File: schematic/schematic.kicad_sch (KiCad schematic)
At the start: 16 parts, among them J1 Conn_01x04, J2 Conn_01x04, J3 Conn_01x04, J4 Conn_01x04, M1 Motor_DC, M2 Motor_DC, M3 Motor_DC, M4 Motor_DC, M5 Motor_Servo, M6 Motor_Servo, U1 BPR-105, U2 BPR-105, U3 BPR-105, U4 BPR-105, U5 LSM9DS1

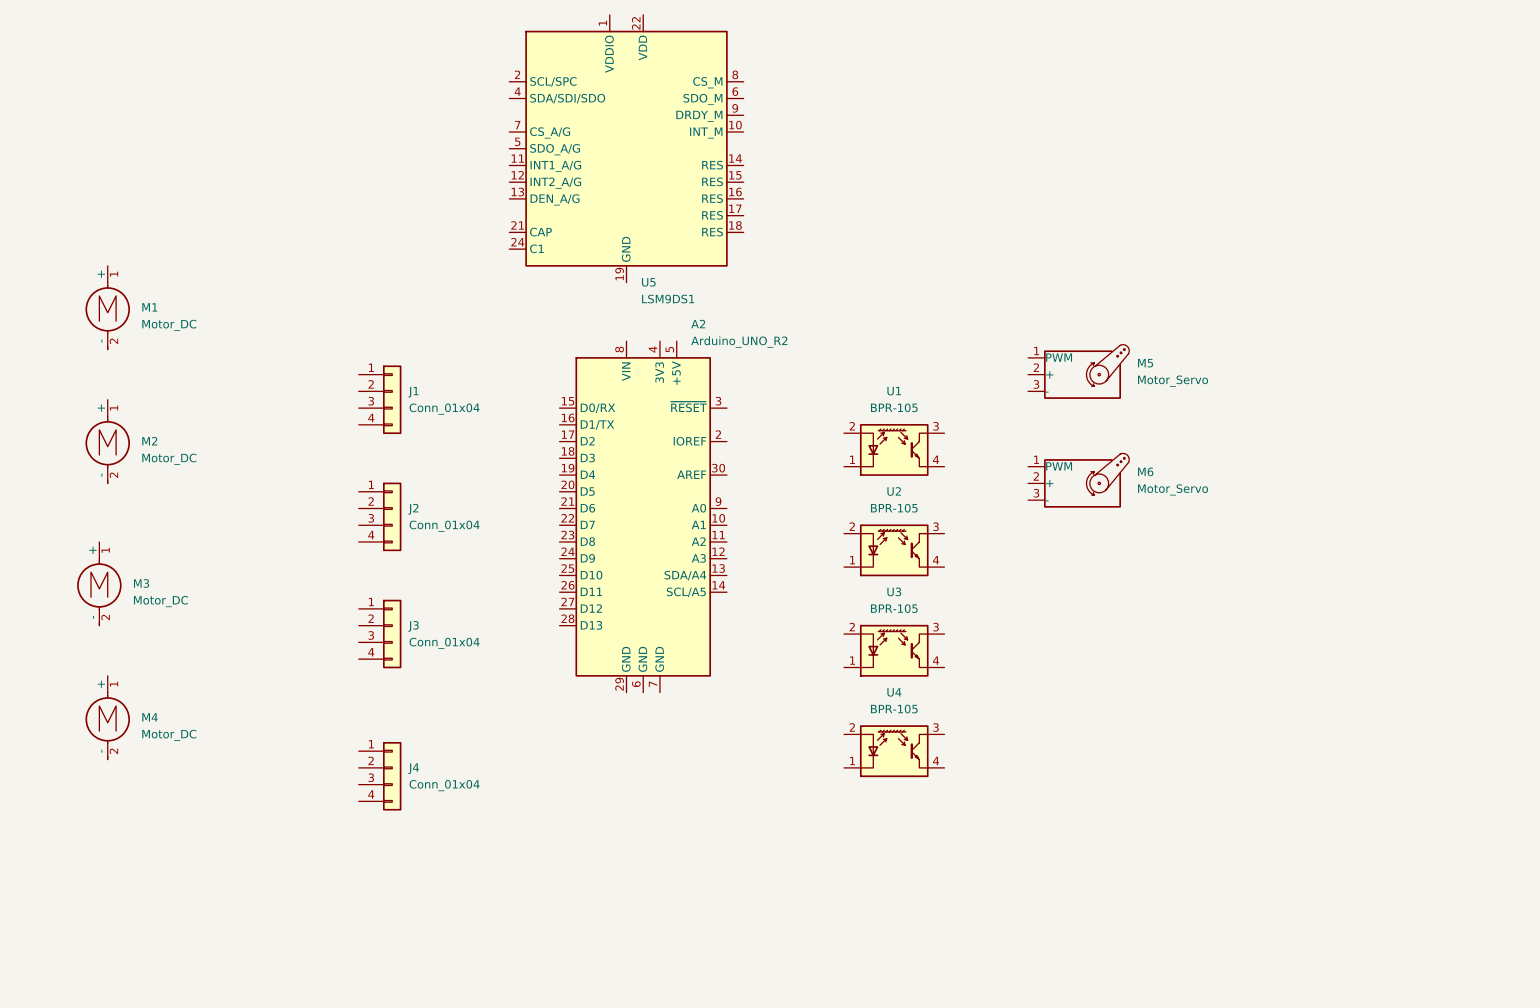
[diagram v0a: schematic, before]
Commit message: added custom symbols for clarity
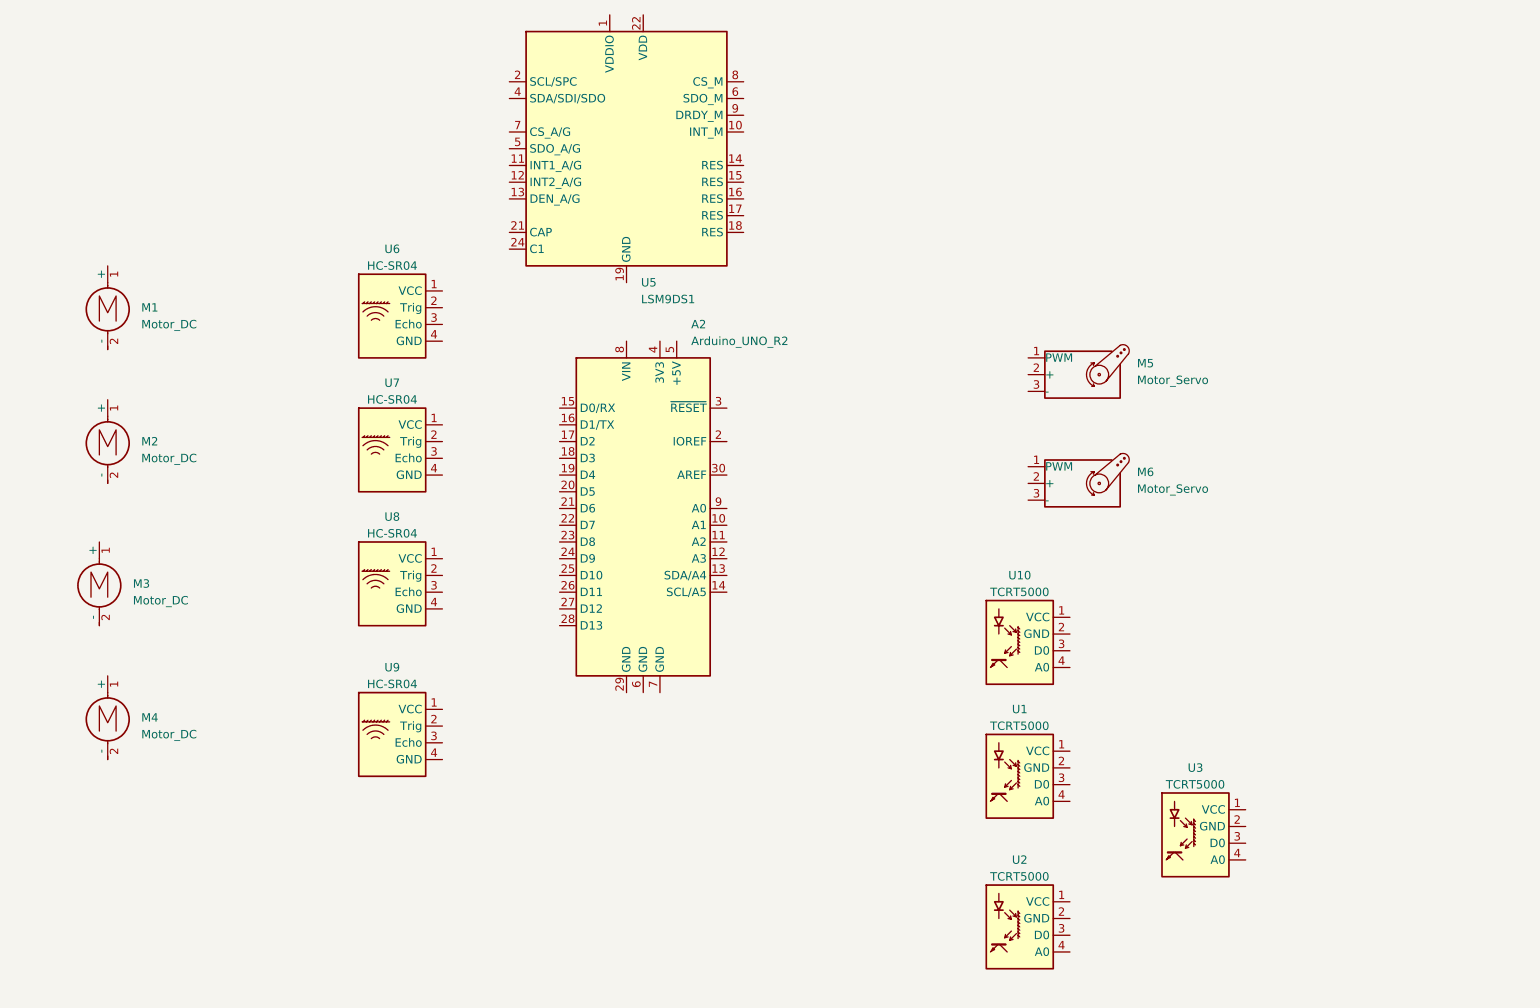
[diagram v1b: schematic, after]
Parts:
- removed J1, J2, J3, J4: Conn_01x04, symbol Connector_Generic:Conn_01x04
- removed U1, U2, U3, U4: BPR-105, OptoDevice:Everlight_ITR8307, symbol Sensor_Proximity:BPR-105
- added U1, U10, U2, U3: TCRT5000, symbol symbol_lib:TCRT5000
- added U6, U7, U8, U9: HC-SR04, symbol symbol_lib:HC-SR04

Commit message: schematic first iter. Running out of pins
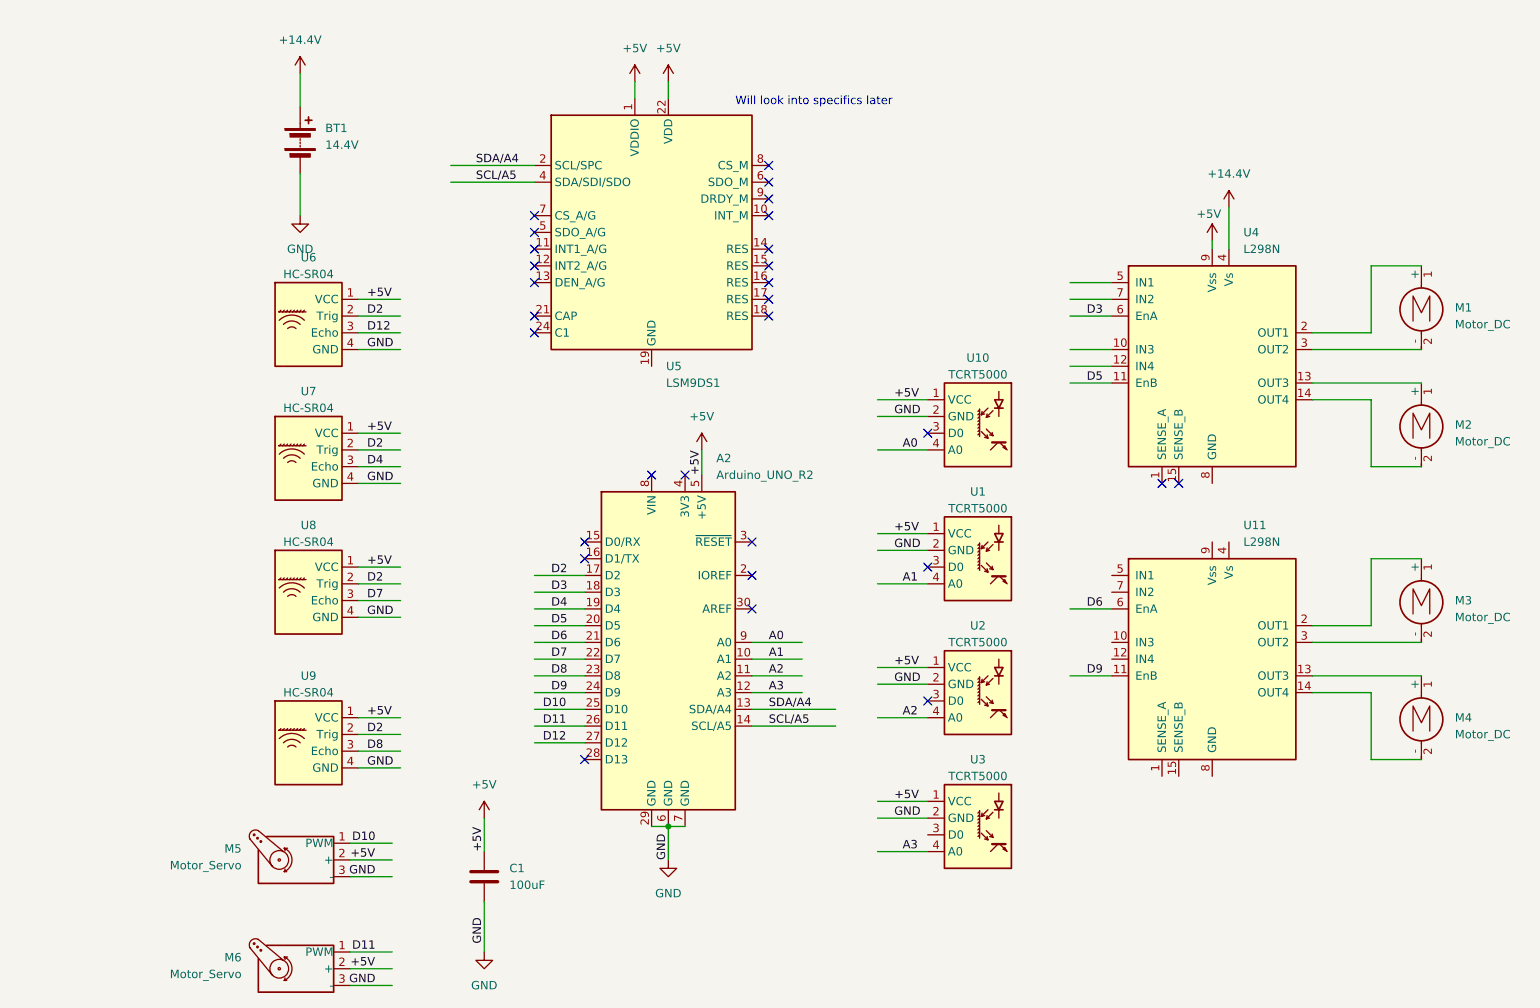
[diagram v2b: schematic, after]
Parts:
- added BT1: 14.4V, symbol Device:Battery
- added C1: 100uF, symbol Device:C
- added U11, U4: L298N, Package_TO_SOT_THT:TO-220-15_P2.54x2.54mm_StaggerOdd_Lead4.58mm_Vertical, symbol Driver_Motor:L298N
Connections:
- net +5V: now reaches U2.1 (VCC)
- net +5V: now also A2.5 (+5V), M5.2 (+), M6.2 (+), U1.1 (VCC), U10.1 (VCC), U3.1 (VCC), U5.1 (VDDIO), U5.22 (VDD), U5.23 (VDD), U5.3 (VDDIO), U6.1 (VCC), U7.1 (VCC), U8.1 (VCC), U9.1 (VCC), C1.1, U4.9 (Vss)
- net GND: now reaches U2.2 (GND)
- net GND: now also A2.29 (GND), A2.6 (GND), A2.7 (GND), M5.3 (-), M6.3 (-), U1.2 (GND), U10.2 (GND), U3.2 (GND), U6.4 (GND), U7.4 (GND), U8.4 (GND), U9.4 (GND), BT1.2 (-), C1.2
- net A2: now reaches U2.4 (A0)
- net A2: now also A2.11 (A2)
- net at M1.1 (+): now also U4.2 (OUT1)
- net at M1.2 (-): now also U4.3 (OUT2)
- net A1: now reaches A2.10 (A1)
- net A1: now also U1.4 (A0)
- net A3: now reaches A2.12 (A3)
- net A3: now also U3.4 (A0)
- net SDA/A4: now reaches A2.13 (SDA/A4)
- net SDA/A4: now also U5.2 (SCL/SPC)
- net SCL/A5: now reaches A2.14 (SCL/A5)
- net SCL/A5: now also U5.4 (SDA/SDI/SDO)
- net D2: now reaches A2.17 (D2)
- net D2: now also U6.2 (Trig), U7.2 (Trig), U8.2 (Trig), U9.2 (Trig)
- net D3: now reaches A2.18 (D3)
- net D3: now also U4.6 (EnA)
- net D4: now reaches A2.19 (D4)
- net D4: now also U7.3 (Echo)
- net D5: now reaches A2.20 (D5)
- net D5: now also U4.11 (EnB)
- net D6: now reaches A2.21 (D6)
- net D6: now also U11.6 (EnA)
- net D7: now reaches A2.22 (D7)
- net D7: now also U8.3 (Echo)
- net D8: now reaches A2.23 (D8)
- net D8: now also U9.3 (Echo)
- net D9: now reaches A2.24 (D9)
- net D9: now also U11.11 (EnB)
- net D10: now reaches A2.25 (D10)
- net D10: now also M5.1 (PWM)
- net D11: now reaches A2.26 (D11)
- net D11: now also M6.1 (PWM)
- net D12: now reaches A2.27 (D12)
- net D12: now also U6.3 (Echo)
- net A0: now reaches A2.9 (A0)
- net A0: now also U10.4 (A0)
- net at M3.1 (+): now also U11.2 (OUT1)
- net at M3.2 (-): now also U11.3 (OUT2)
- net at M4.1 (+): now also U11.13 (OUT3)
- net at M4.2 (-): now also U11.14 (OUT4)
- net at M2.1 (+): now also U4.13 (OUT3)
- net at M2.2 (-): now also U4.14 (OUT4)
- new net +14.4V: BT1.1 (+), U4.4 (Vs)
- no-connect marks 0 -> 29
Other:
- note added: "Will look into specifics later"
- moved on the sheet: A2, M1, M2, M5, M6, U1, U10, U2, U3, U5, U6, U7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

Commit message: schematic updated
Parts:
- removed A2: Arduino_UNO_R2, Module:Arduino_UNO_R2, symbol MCU_Module:Arduino_UNO_R2
- removed C1: 100uF, symbol Device:C
- removed M1, M2, M3, M4: Motor_DC, symbol Motor:Motor_DC
- removed M5, M6: Motor_Servo, symbol Motor:Motor_Servo
- removed U1, U10, U2, U3: TCRT5000, symbol symbol_lib:TCRT5000
- removed U11, U4: L298N, Package_TO_SOT_THT:TO-220-15_P2.54x2.54mm_StaggerOdd_Lead4.58mm_Vertical, symbol Driver_Motor:L298N
- removed U5: LSM9DS1, Package_LGA:LGA-24L_3x3.5mm_P0.43mm, symbol Sensor_Motion:LSM9DS1
- removed U6, U7, U8, U9: HC-SR04, symbol symbol_lib:HC-SR04
- added U16: LM2596S-5, Package_TO_SOT_SMD:TO-263-5_TabPin3, symbol Regulator_Switching:LM2596S-5
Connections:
- net +14.4V: now also U16.1 (VIN)
- net +5V: now also U16.2 (OUT), U16.4 (FB)
- net GND: now also U16.3 (GND), U16.5 (~{ON}/OFF)
- no-connect marks 29 -> 0
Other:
- added sheet master_mcu (master_mcu.kicad_sch)
- added sheet peripheral_mcu (peripheral_mcu.kicad_sch)
- note removed: "Will look into specifics later"
- moved on the sheet: BT1

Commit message: updated schematic
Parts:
- renumbered U16 to U1
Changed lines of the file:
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@@
 		(dnp no)
 		(fields_autoplaced yes)
-		(property "Reference" "#PWR045"
+		(property "Reference" "#PWR05"
 			(at 96.52 52.07 0)
 			(effects
@@
 			(project ""
 				(path "/a117cae9-da48-465a-8dd5-c903415f43a6"
-					(reference "#PWR045")
+					(reference "#PWR05")
 					(unit 1)
 				)
@@
 		(dnp no)
 		(fields_autoplaced yes)
-		(property "Reference" "#PWR046"
+		(property "Reference" "#PWR04"
 			(at 80.01 68.58 0)
 			(effects
@@
 			(project "schematic"
 				(path "/a117cae9-da48-465a-8dd5-c903415f43a6"
-					(reference "#PWR046")
+					(reference "#PWR04")
 					(unit 1)
 				)
@@
 		(dnp no)
 		(fields_autoplaced yes)
-		(property "Reference" "#PWR04"
+		(property "Reference" "#PWR02"
 			(at 44.45 72.39 0)
 			(effects
@@
 			(project ""
 				(path "/a117cae9-da48-465a-8dd5-c903415f43a6"
-					(reference "#PWR04")
+					(reference "#PWR02")
 					(unit 1)
 				)
@@
 		(dnp no)
 		(fields_autoplaced yes)
-		(property "Reference" "#PWR047"
+		(property "Reference" "#PWR03"
 			(at 63.5 52.07 0)
 			(effects
@@
 			(project "schematic"
 				(path "/a117cae9-da48-465a-8dd5-c903415f43a6"
-					(reference "#PWR047")
+					(reference "#PWR03")
 					(unit 1)
 				)
@@
 		(dnp no)
 		(fields_autoplaced yes)
-		(property "Reference" "U16"
+		(property "Reference" "U1"
 			(at 80.01 44.45 0)
 			(effects
@@
 			(project ""
 				(path "/a117cae9-da48-465a-8dd5-c903415f43a6"
-					(reference "U16")
+					(reference "U1")
 					(unit 1)
 				)
@@
 		(dnp no)
 		(fields_autoplaced yes)
-		(property "Reference" "#PWR03"
+		(property "Reference" "#PWR01"
 			(at 44.45 48.26 0)
 			(effects
@@
 			(project ""
 				(path "/a117cae9-da48-465a-8dd5-c903415f43a6"
-					(reference "#PWR03")
-					(unit 1)
-				)
+					(reference "#PWR01")
+					(unit 1)
+				)

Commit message: update schematics
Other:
- sheet master_mcu renamed core_Ccu
- sheet peripheral_mcu renamed peripheral_Ccu
- sheet core_Ccu: file master_mcu.kicad_sch -> core_Ccu.kicad_Pch
- sheet peripheral_Ccu: file peripheral_mcu.kicad_sch -> peripheral_Ccu.kicad_Pch
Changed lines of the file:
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@@
 			(color 0 0 0 0.0000)
 		)
-		(property "Sheetname" "master_mcu"
+		(property "Sheetname" "core_Ccu"
 			(at 105.41 39.9284 0)
 			(effects
@@
 			)
 		)
-		(property "Sheetfile" "master_mcu.kicad_sch"
+		(property "Sheetfile" "core_Ccu.kicad_Pch"
 			(at 105.41 62.8146 0)
 			(effects
@@
 			(color 0 0 0 0.0000)
 		)
-		(property "Sheetname" "peripheral_mcu"
+		(property "Sheetname" "peripheral_Ccu"
 			(at 138.43 40.5634 0)
 			(effects
@@
 			)
 		)
-		(property "Sheetfile" "peripheral_mcu.kicad_sch"
+		(property "Sheetfile" "peripheral_Ccu.kicad_Pch"
 			(at 138.43 62.1796 0)
 			(effects

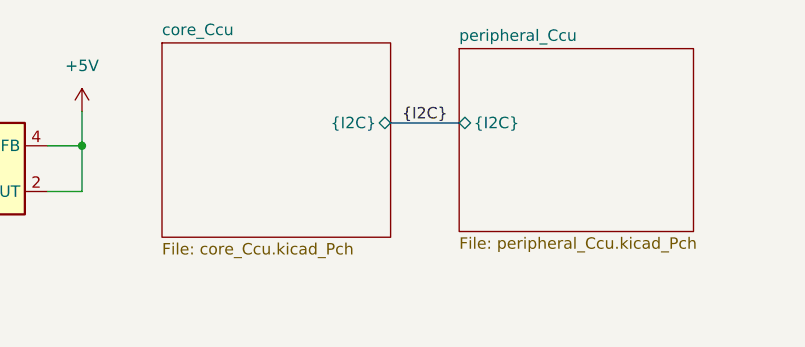
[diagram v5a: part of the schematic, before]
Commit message: schematic update
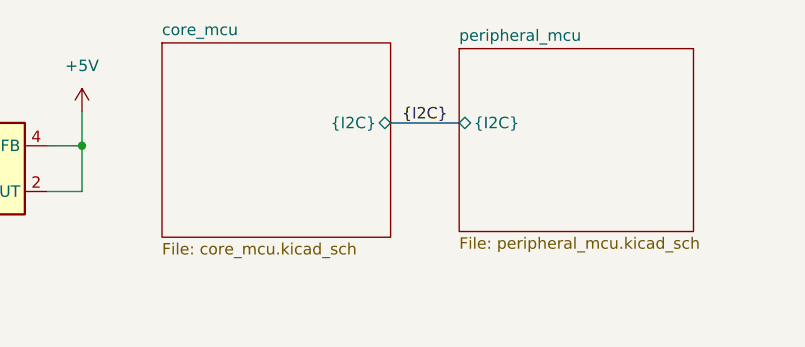
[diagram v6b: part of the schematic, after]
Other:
- sheet core_Ccu renamed core_mcu
- sheet peripheral_Ccu renamed peripheral_mcu
- sheet core_mcu: file core_Ccu.kicad_Pch -> core_mcu.kicad_sch
- sheet peripheral_mcu: file peripheral_Ccu.kicad_Pch -> peripheral_mcu.kicad_sch
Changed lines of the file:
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@@
 			(color 0 0 0 0.0000)
 		)
-		(property "Sheetname" "core_Ccu"
+		(property "Sheetname" "core_mcu"
 			(at 105.41 39.9284 0)
 			(effects
@@
 			)
 		)
-		(property "Sheetfile" "core_Ccu.kicad_Pch"
+		(property "Sheetfile" "core_mcu.kicad_sch"
 			(at 105.41 62.8146 0)
 			(effects
@@
 			(color 0 0 0 0.0000)
 		)
-		(property "Sheetname" "peripheral_Ccu"
+		(property "Sheetname" "peripheral_mcu"
 			(at 138.43 40.5634 0)
 			(effects
@@
 			)
 		)
-		(property "Sheetfile" "peripheral_Ccu.kicad_Pch"
+		(property "Sheetfile" "peripheral_mcu.kicad_sch"
 			(at 138.43 62.1796 0)
 			(effects

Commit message: update schematic to match most recent config
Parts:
- added C7, C9: 0.1uF, symbol Device:C
- added C8: 0.22uF, symbol Device:C
- added F1: Fuse, symbol Device:Fuse
- added SW1: SW_SPST, symbol Switch:SW_SPST
- added U16: L7805, symbol Regulator_Linear:L7805
- U1: value LM2596S-5 -> LM2596S-12
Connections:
- net +14.4V: now also SW1.2 (B); no longer BT1.1 (+)
- net +5V: now also C9.1, U16.3 (OUT); no longer U1.2 (OUT), U1.4 (FB)
- net GND: now also C7.2, C8.1, C9.2, U16.2 (GND)
- new net: BT1.1 (+), F1.1
- new net: F1.2, SW1.1 (A)
- new net +12V: C7.1, C8.2, U1.2 (OUT), U1.4 (FB), U16.1 (IN)
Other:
- note added: "Power Management"
- moved on the sheet: BT1, U1
